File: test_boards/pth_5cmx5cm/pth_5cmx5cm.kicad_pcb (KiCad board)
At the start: 2 copper layers, 49.5 x 49.5 mm, 9 parts, among them Q101 BC560, Q102 2N3904, U101 4N35

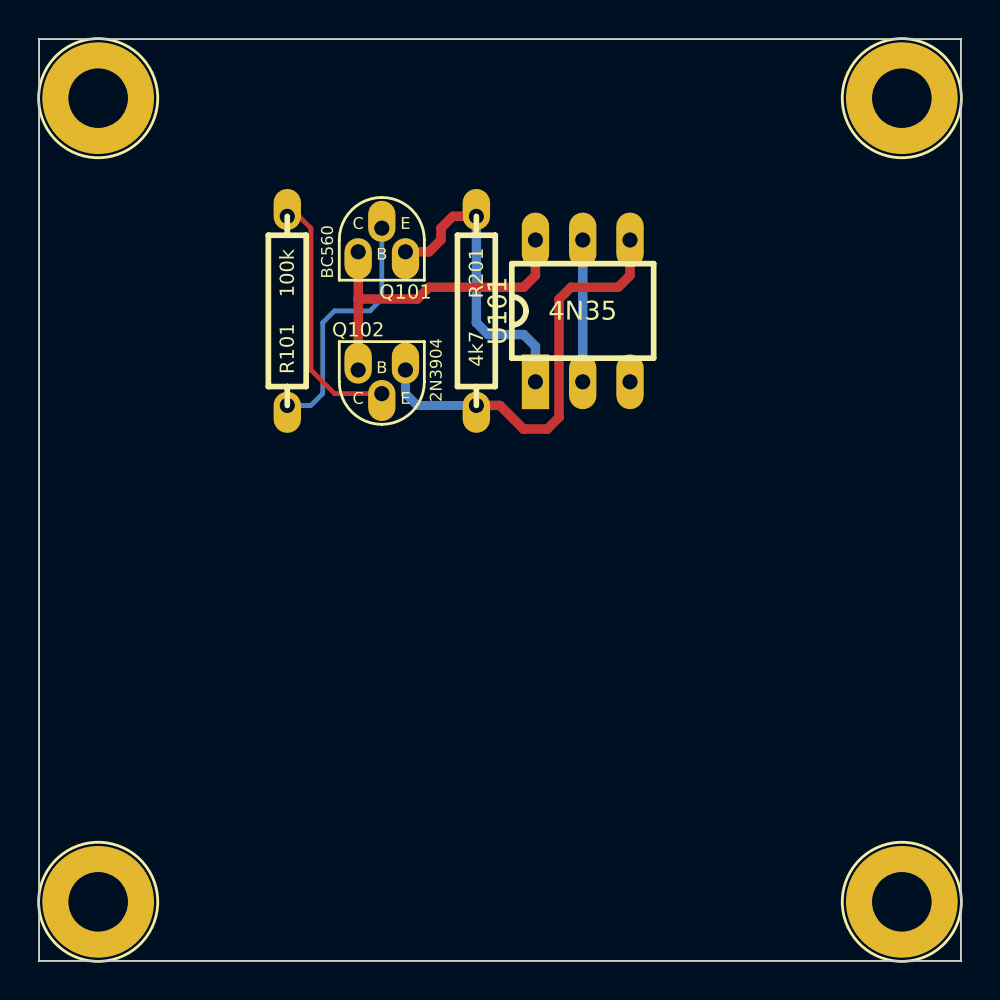
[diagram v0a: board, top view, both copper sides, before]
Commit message: pulling in OSHW-logo.mod (can't remember where I downloaded this from now...), reducing the number of logo options, and fixing the layers for the rest of the logos.  updating demo board.
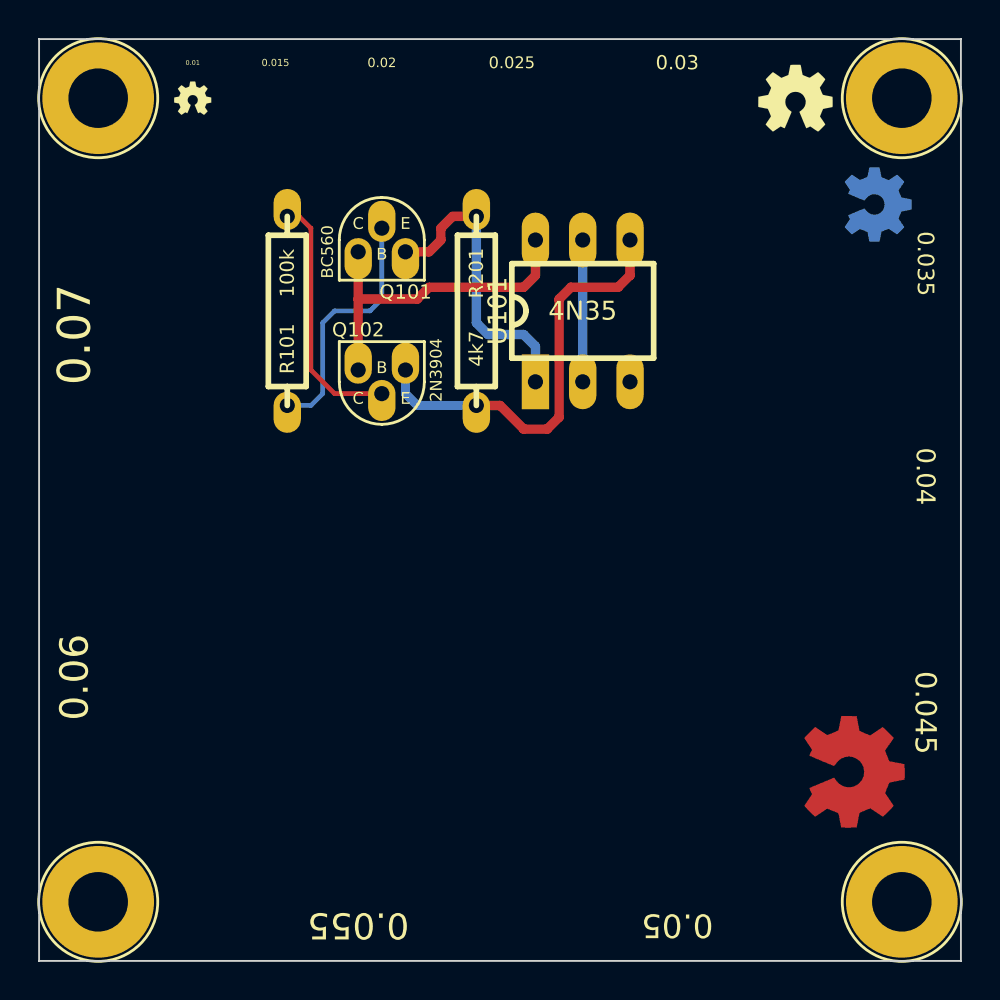
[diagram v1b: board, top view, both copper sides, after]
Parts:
- added G***: OSHW-logo_silkscreen-front_4mm, OSHW-logo_silkscreen-front_4mm, F.Cu at (237.5, 111.1)
- added G***: OSHW-logo_silkscreen-front_2mm, OSHW-logo_silkscreen-front_2mm, F.Cu at (205.1, 111.1)
- added G***: OSHW-logo_silkscreen-back_10mm, OSHW-logo_silkscreen-back_10mm, F.Cu at (208.9, 152.4)
- added G***: OSHW-logo_silkscreen-back_6mm, OSHW-logo_silkscreen-back_6mm, F.Cu at (236.2, 154.3)
- added G***: OSHW-logo_copper-back_4mm, OSHW-logo_copper-back_4mm, F.Cu at (241.9, 116.8)
- added G***: OSHW-logo_copper-front_6mm, OSHW-logo_copper-front_6mm, F.Cu at (240.7, 147.3)
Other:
- board text added: "0.01"
- board text added: "0.015"
- board text added: "0.02"
- board text added: "0.025"
- board text added: "0.03"
- board text added: "0.035"
- board text added: "0.04"
- board text added: "0.045"
- board text added: "0.05"
- board text added: "0.055"
- board text added: "0.06"
- board text added: "0.07"
